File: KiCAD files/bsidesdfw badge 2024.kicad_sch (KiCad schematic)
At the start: 43 parts, among them Q1 BC548, U1 NE555P, U2 74HC595

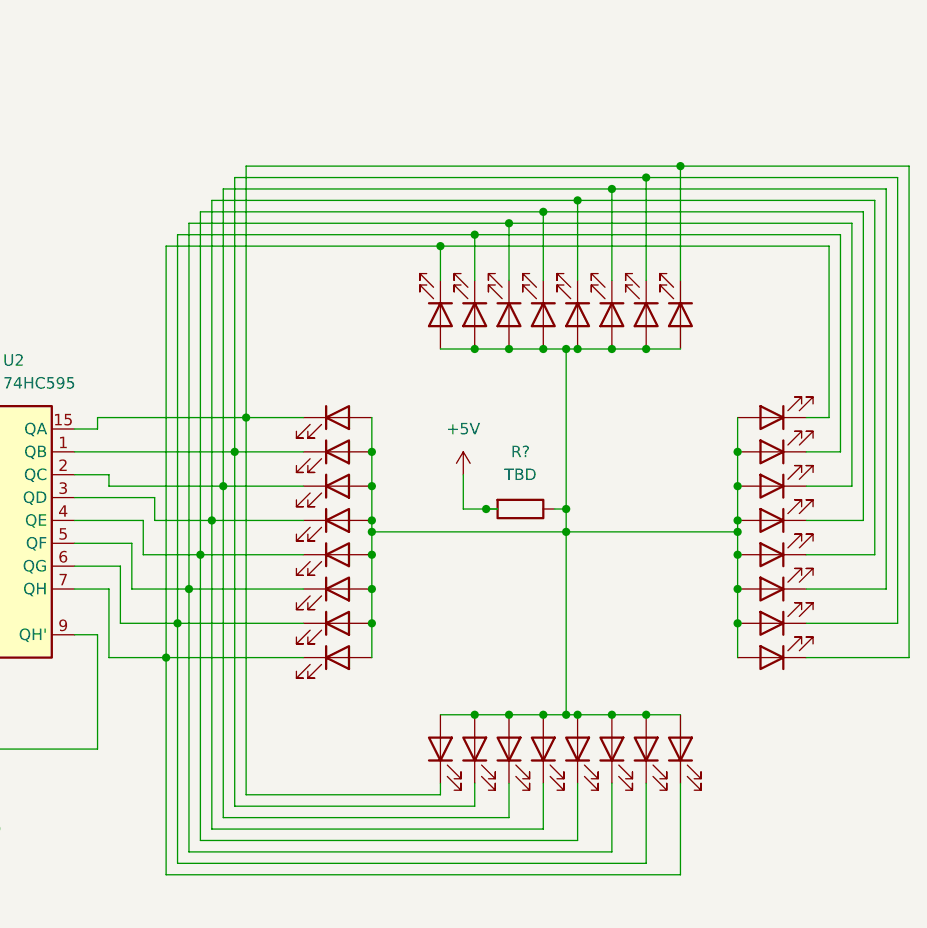
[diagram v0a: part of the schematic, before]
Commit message: updated number of LEDs
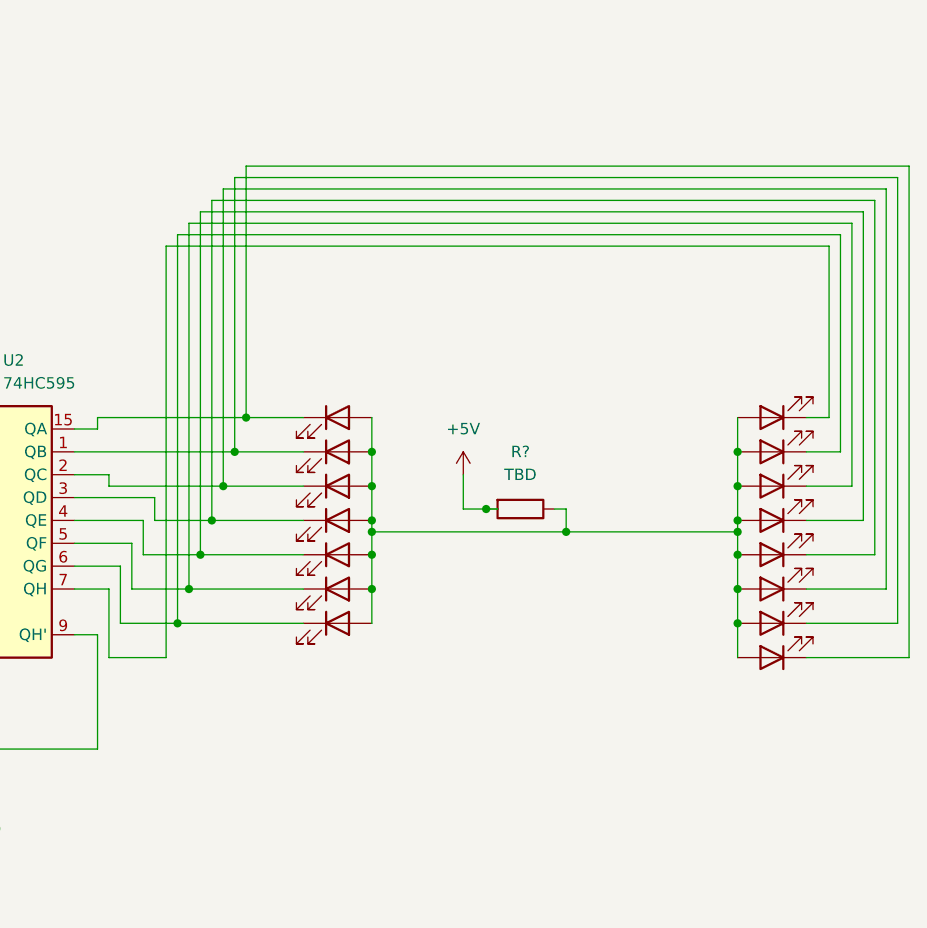
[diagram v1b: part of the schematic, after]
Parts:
- removed D10, D11, D12, D13, D14, D15, D16, D17, D18, D19, D20, D21, D22, D23, D24, D8, D9: ~, symbol Device:LED

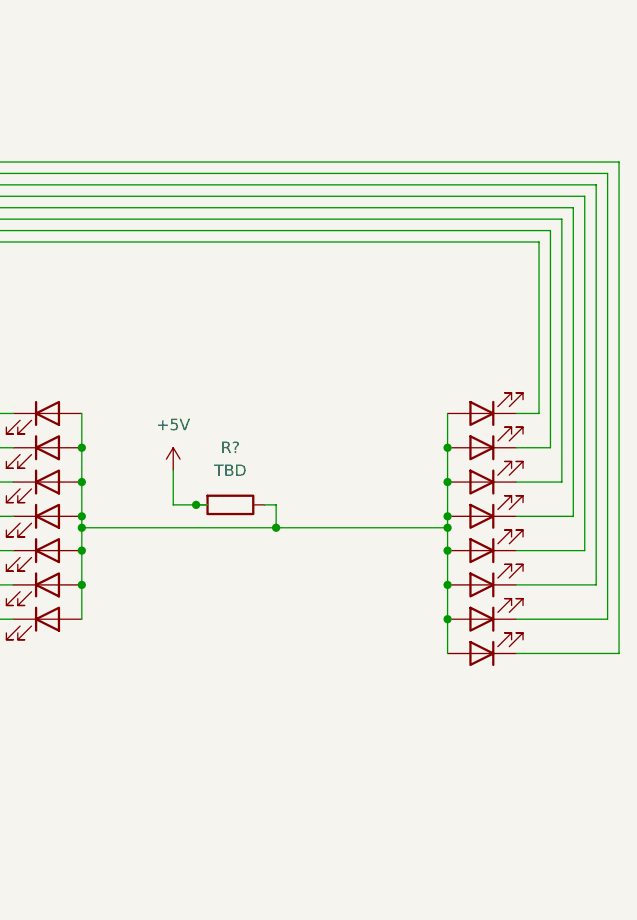
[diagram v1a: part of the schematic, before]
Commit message: LEDs picked, resistor values updated
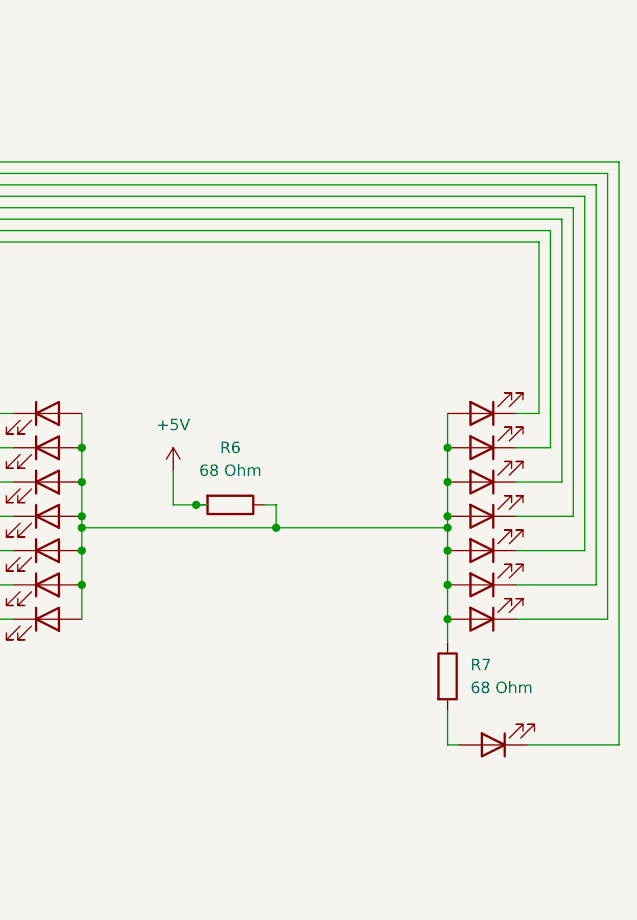
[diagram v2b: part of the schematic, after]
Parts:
- added R7: 68 Ohm, symbol Device:R
- R6: renamed from R?; value TBD -> 68 Ohm
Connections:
- net at D1.2 (A), D2.2 (A), D25.2 (A)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: now also R7.1; no longer D32.2 (A)
- new net: D32.2 (A), R7.2
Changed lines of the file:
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@@
+	)
+	(junction
+		(at 236.22 116.84)
+		(diameter 0)
+		(color 0 0 0 0)
 	)
 	(junction
@@
 	)
 	(junction
-		(at 236.22 116.84)
-		(diameter 0)
-		(color 0 0 0 0)
-	)
-	(junction
 		(at 195.58 109.22)
 		(diameter 0)
@@
 	(wire
 		(pts
+			(xy 236.22 127) (xy 236.22 130.81)
+		)
+		(stroke
+			(width 0)
+			(type default)
+		)
+	)
+	(wire
+		(pts
 			(xy 114.3 130.81) (xy 165.1 130.81)
 		)
@@
 	(wire
 		(pts
+			(xy 236.22 130.81) (xy 237.49 130.81)
+		)
+		(stroke
+			(width 0)
+			(type default)
+		)
+	)
+	(wire
+		(pts
 			(xy 176.53 71.12) (xy 176.53 109.22)
 		)
@@
 	(wire
 		(pts
-			(xy 236.22 116.84) (xy 236.22 120.65)
-		)
-		(stroke
-			(width 0)
-			(type default)
-		)
-	)
-	(wire
-		(pts
 			(xy 173.99 73.66) (xy 247.65 73.66)
 		)
@@
 	(wire
 		(pts
+			(xy 236.22 116.84) (xy 236.22 119.38)
+		)
+		(stroke
+			(width 0)
+			(type default)
+		)
+	)
+	(wire
+		(pts
 			(xy 181.61 93.98) (xy 187.96 93.98)
 		)
@@
 	(wire
 		(pts
-			(xy 255.27 120.65) (xy 255.27 66.04)
-		)
-		(stroke
-			(width 0)
-			(type default)
-		)
-	)
-	(wire
-		(pts
-			(xy 243.84 120.65) (xy 255.27 120.65)
+			(xy 255.27 130.81) (xy 255.27 66.04)
+		)
+		(stroke
+			(width 0)
+			(type default)
+		)
+	)
+	(wire
+		(pts
+			(xy 245.11 130.81) (xy 255.27 130.81)
 		)
 		(stroke
@@
 		(dnp no)
 		(fields_autoplaced yes)
-		(property "Reference" "R?"
+		(property "Reference" "R6"
 			(at 212.09 97.79 90)
 			(effects
@@
 			)
 		)
-		(property "Value" "TBD"
+		(property "Value" "68 Ohm"
 			(at 212.09 100.33 90)
 			(effects
@@
 			(project ""
 				(path "/b322d770-db2f-42fe-b67c-63c256de8558"
-					(reference "R?")
+					(reference "R6")
 					(unit 1)
 				)
@@
 	(symbol
 		(lib_id "Device:R")
+		(at 236.22 123.19 0)
+		(unit 1)
+		(exclude_from_sim no)
+		(in_bom yes)
+		(on_board yes)
+		(dnp no)
+		(fields_autoplaced yes)
+		(property "Reference" "R7"
+			(at 238.76 121.9199 0)
+			(effects
+				(font
+					(size 1.27 1.27)
+				)
+				(justify left)
+			)
+		)
+		(property "Value" "68 Ohm"
+			(at 238.76 124.4599 0)
+			(effects
+				(font
+					(size 1.27 1.27)
+				)
+				(justify left)
+			)
+		)
+		(property "Footprint" ""
+			(at 234.442 123.19 90)
+			(effects
+				(font
+					(size 1.27 1.27)
+				)
+				(hide yes)
+			)
+		)
+		(property "Datasheet" "~"
+			(at 236.22 123.19 0)
+			(effects
+				(font
+					(size 1.27 1.27)
+				)
+				(hide yes)
+			)
+		)
+		(property "Description" "Resistor"
+			(at 236.22 123.19 0)
+			(effects
+				(font
+					(size 1.27 1.27)
+				)
+				(hide yes)
+			)
+		)
+		(pin "1"
+		)
+		(pin "2"
+		)
+		(instances
+			(project "bsidesdfw badge 2024"
+				(path "/b322d770-db2f-42fe-b67c-63c256de8558"
+					(reference "R7")
+					(unit 1)
+				)
+			)
+		)
+	)
+	(symbol
+		(lib_id "Device:R")
 		(at 63.5 116.84 0)
 		(unit 1)
@@
 	(symbol
 		(lib_id "Device:LED")
-		(at 240.03 120.65 180)
+		(at 241.3 130.81 180)
 		(unit 1)
 		(exclude_from_sim no)
@@
 		(fields_autoplaced yes)
 		(property "Reference" "D32"
-			(at 241.6176 123.19 90)
+			(at 242.8876 133.35 90)
 			(effects
 				(font
@@
 		)
 		(property "Value" "~"
-			(at 241.6175 123.19 0)
+			(at 242.8875 133.35 0)
 			(effects
 				(font
@@
 		)
 		(property "Footprint" ""
-			(at 240.03 120.65 0)
+			(at 241.3 130.81 0)
 			(effects
 				(font
@@
 		)
 		(property "Datasheet" "~"
-			(at 240.03 120.65 0)
+			(at 241.3 130.81 0)
 			(effects
 				(font
@@
 		)
 		(property "Description" "Light emitting diode"
-			(at 240.03 120.65 0)
-			(effects
-				(font
+			(at 241.3 130.81 0)
+			(effects
+				(font

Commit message: part models. trim pot needs model created
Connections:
- net +5V renamed +6V
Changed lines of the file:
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@@
 			)
 		)
-		(property "Value" "+5V"
-			(at 116.84 102.87 0)
+		(property "Value" "+6V"
+			(at 120.65 100.33 90)
 			(effects
 				(font
@@
 			)
 		)
-		(property "Value" "+5V"
-			(at 205.74 95.25 0)
-			(effects
-				(font
-					(size 1.27 1.27)
-				)
+		(property "Value" "+6V"
+			(at 208.28 99.0599 0)
+			(effects
+				(font
+					(size 1.27 1.27)
+				)
+				(justify left)
 			)
 		)
@@
 			)
 		)
-		(property "Value" "+5V"
-			(at 152.4 80.01 0)
-			(effects
-				(font
-					(size 1.27 1.27)
-				)
+		(property "Value" "+6V"
+			(at 154.94 83.8199 0)
+			(effects
+				(font
+					(size 1.27 1.27)
+				)
+				(justify left)
 			)
 		)
@@
 			)
 		)
-		(property "Value" "+5V"
-			(at 72.39 99.06 0)
-			(effects
-				(font
-					(size 1.27 1.27)
-				)
-			)
-		)
+		(property "Value" "+6V"
+			(at 74.93 102.8699 0)
+			(effects
+				(font
+					(size 1.27 1.27)
+				)
+				(justify left)
+			)
+		)

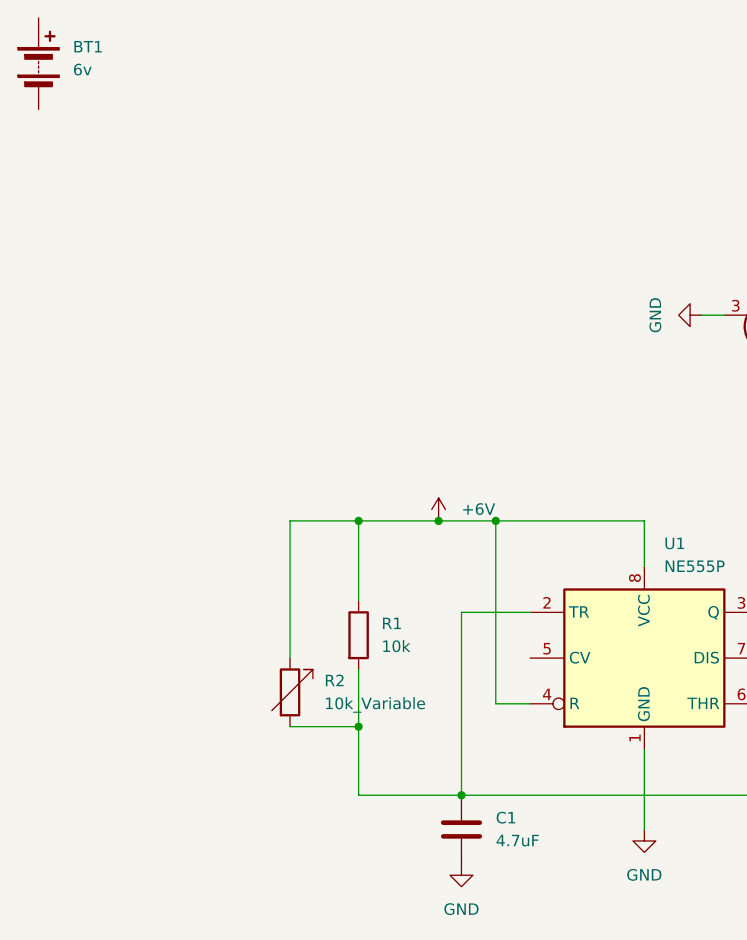
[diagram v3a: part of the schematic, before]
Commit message: corrected the pin numbering for the trim resistor footprint; updated schematic to reflect trim properly
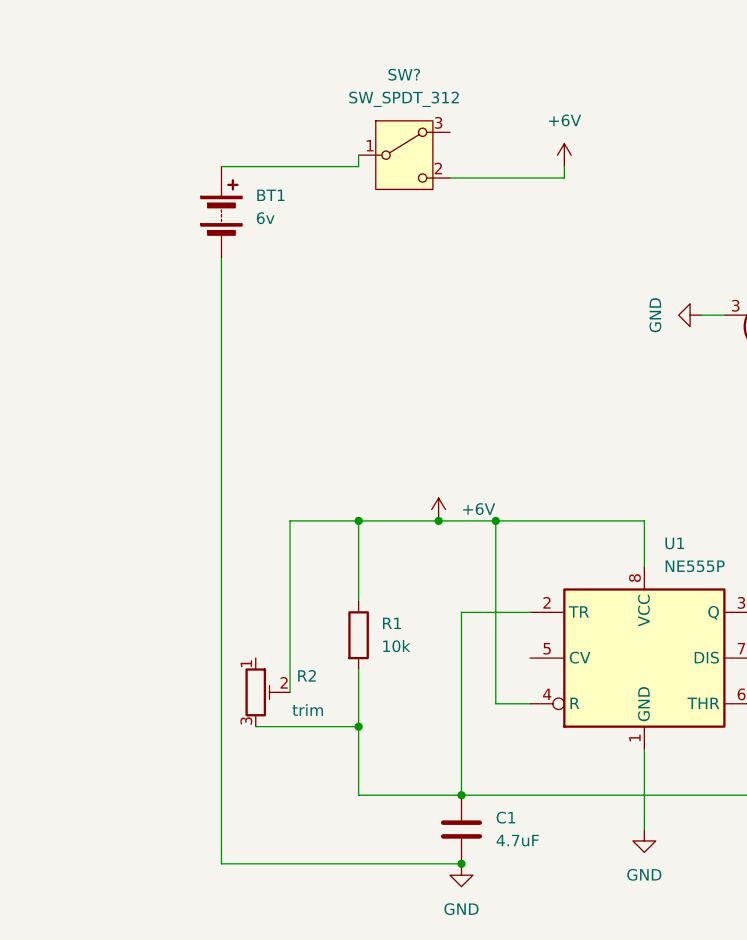
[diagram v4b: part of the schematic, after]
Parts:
- removed R2: 10k_Variable, symbol Device:R_Variable
- added R2: trim, symbol Device:R_Potentiometer_Trim
- added SW?: SW_SPDT_312, symbol Switch:SW_SPDT_312
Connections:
- net +6V: now also R2.2, SW?.2 (C)
- net GND: now also BT1.2 (-)
- net at BT1.1 (+): now also SW?.1 (B)
- net at C1.1, R1.2, U1.2 (TR)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: now also R2.3
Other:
- moved on the sheet: BT1
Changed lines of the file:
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@@
 	)
 	(junction
+		(at 74.93 142.24)
+		(diameter 0)
+		(color 0 0 0 0)
+	)
+	(junction
 		(at 236.22 116.84)
 		(diameter 0)
@@
 	(wire
 		(pts
+			(xy 63.5 64.77) (xy 63.5 63.5)
+		)
+		(stroke
+			(width 0)
+			(type default)
+		)
+	)
+	(wire
+		(pts
 			(xy 236.22 130.81) (xy 237.49 130.81)
 		)
@@
 	(wire
 		(pts
+			(xy 48.26 142.24) (xy 74.93 142.24)
+		)
+		(stroke
+			(width 0)
+			(type default)
+		)
+	)
+	(wire
+		(pts
 			(xy 176.53 71.12) (xy 176.53 109.22)
 		)
@@
 	(wire
 		(pts
+			(xy 48.26 74.93) (xy 48.26 142.24)
+		)
+		(stroke
+			(width 0)
+			(type default)
+		)
+	)
+	(wire
+		(pts
 			(xy 152.4 85.09) (xy 152.4 90.17)
 		)
@@
 	(wire
 		(pts
+			(xy 52.07 127) (xy 63.5 127)
+		)
+		(stroke
+			(width 0)
+			(type default)
+		)
+	)
+	(wire
+		(pts
 			(xy 72.39 104.14) (xy 78.74 104.14)
 		)
@@
 	(wire
 		(pts
-			(xy 63.5 127) (xy 55.88 127)
-		)
-		(stroke
-			(width 0)
-			(type default)
-		)
-	)
-	(wire
-		(pts
 			(xy 107.95 114.3) (xy 129.54 114.3)
 		)
@@
 	(wire
 		(pts
+			(xy 73.66 66.04) (xy 86.36 66.04)
+		)
+		(stroke
+			(width 0)
+			(type default)
+		)
+	)
+	(wire
+		(pts
 			(xy 177.8 69.85) (xy 177.8 105.41)
 		)
@@
 	(wire
 		(pts
+			(xy 48.26 64.77) (xy 63.5 64.77)
+		)
+		(stroke
+			(width 0)
+			(type default)
+		)
+	)
+	(wire
+		(pts
 			(xy 195.58 105.41) (xy 195.58 106.68)
 		)
@@
 	(wire
 		(pts
+			(xy 86.36 66.04) (xy 86.36 64.77)
+		)
+		(stroke
+			(width 0)
+			(type default)
+		)
+	)
+	(wire
+		(pts
 			(xy 123.19 95.25) (xy 123.19 102.87)
 		)
@@
 	(wire
 		(pts
-			(xy 55.88 119.38) (xy 55.88 104.14)
+			(xy 55.88 104.14) (xy 55.88 123.19)
 		)
 		(stroke
@@
 	(symbol
 		(lib_id "Device:Battery")
-		(at 27.94 53.34 0)
+		(at 48.26 69.85 0)
 		(unit 1)
 		(exclude_from_sim no)
@@
 		(fields_autoplaced yes)
 		(property "Reference" "BT1"
-			(at 31.75 51.4984 0)
+			(at 52.07 68.0084 0)
 			(effects
 				(font
@@
 		)
 		(property "Value" "6v"
-			(at 31.75 54.0384 0)
+			(at 52.07 70.5484 0)
 			(effects
 				(font
@@
 		)
 		(property "Footprint" ""
-			(at 27.94 51.816 90)
+			(at 48.26 68.326 90)
 			(effects
 				(font
@@
 		)
 		(property "Datasheet" "~"
-			(at 27.94 51.816 90)
+			(at 48.26 68.326 90)
 			(effects
 				(font
@@
 		)
 		(property "Description" "Multiple-cell battery"
-			(at 27.94 53.34 0)
+			(at 48.26 69.85 0)
 			(effects
 				(font
@@
 	)
 	(symbol
+		(lib_id "power:+5V")
+		(at 86.36 64.77 0)
+		(unit 1)
+		(exclude_from_sim no)
+		(in_bom yes)
+		(on_board yes)
+		(dnp no)
+		(fields_autoplaced yes)
+		(property "Reference" "#PWR09"
+			(at 86.36 68.58 0)
+			(effects
+				(font
+					(size 1.27 1.27)
+				)
+				(hide yes)
+			)
+		)
+		(property "Value" "+6V"
+			(at 86.36 59.69 0)
+			(effects
+				(font
+					(size 1.27 1.27)
+				)
+			)
+		)
+		(property "Footprint" ""
+			(at 86.36 64.77 0)
+			(effects
+				(font
+					(size 1.27 1.27)
+				)
+				(hide yes)
+			)
+		)
+		(property "Datasheet" ""
+			(at 86.36 64.77 0)
+			(effects
+				(font
+					(size 1.27 1.27)
+				)
+				(hide yes)
+			)
+		)
+		(property "Description" "Power symbol creates a global label with name \"+5V\""
+			(at 86.36 64.77 0)
+			(effects
+				(font
+					(size 1.27 1.27)
+				)
+				(hide yes)
+			)
+		)
+		(pin "1"
+		)
+		(instances
+			(project ""
+				(path "/b322d770-db2f-42fe-b67c-63c256de8558"
+					(reference "#PWR09")
+					(unit 1)
+				)
+			)
+		)
+	)
+	(symbol
 		(lib_id "Device:R")
 		(at 236.22 123.19 0)
@@
 	)
 	(symbol
+		(lib_id "Device:R_Potentiometer_Trim")
+		(at 52.07 123.19 0)
+		(unit 1)
+		(exclude_from_sim no)
+		(in_bom yes)
+		(on_board yes)
+		(dnp no)
+		(property "Reference" "R2"
+			(at 58.928 121.412 0)
+			(effects
+				(font
+					(size 1.27 1.27)
+				)
+				(justify right)
+			)
+		)
+		(property "Value" "trim"
+			(at 59.69 125.222 0)
+			(effects
+				(font
+					(size 1.27 1.27)
+				)
+				(justify right)
+			)
+		)
+		(property "Footprint" ""
+			(at 52.07 123.19 0)
+			(effects
+				(font
+					(size 1.27 1.27)
+				)
+				(hide yes)
+			)
+		)
+		(property "Datasheet" "~"
+			(at 52.07 123.19 0)
+			(effects
+				(font
+					(size 1.27 1.27)
+				)
+				(hide yes)
+			)
+		)
+		(property "Description" "Trim-potentiometer"
+			(at 52.07 123.19 0)
+			(effects
+				(font
+					(size 1.27 1.27)
+				)
+				(hide yes)
+			)
+		)
+		(pin "1"
+		)
+		(pin "3"
+		)
+		(pin "2"
+		)
+		(instances
+			(project ""
+				(path "/b322d770-db2f-42fe-b67c-63c256de8558"
+					(reference "R2")
+					(unit 1)
+				)
+			)
+		)
+	)
+	(symbol
 		(lib_id "74xx:74HC595")
 		(at 152.4 105.41 0)
@@
 	)
 	(symbol
+		(lib_id "Switch:SW_SPDT_312")
+		(at 68.58 63.5 0)
+		(unit 1)
+		(exclude_from_sim no)
+		(in_bom yes)
+		(on_board yes)
+		(dnp no)
+		(fields_autoplaced yes)
+		(property "Reference" "SW?"
+			(at 68.58 54.61 0)
+			(effects
+				(font
+					(size 1.27 1.27)
+				)
+			)
+		)
+		(property "Value" "SW_SPDT_312"
+			(at 68.58 57.15 0)
+			(effects
+				(font
+					(size 1.27 1.27)
+				)
+			)
+		)
+		(property "Footprint" ""
+			(at 68.58 73.66 0)
+			(effects
+				(font
+					(size 1.27 1.27)
+				)
+				(hide yes)
+			)
+		)
+		(property "Datasheet" "~"
+			(at 68.58 71.12 0)
+			(effects
+				(font
+					(size 1.27 1.27)
+				)
+				(hide yes)
+			)
+		)
+		(property "Description" "Switch, single pole double throw"
+			(at 68.58 63.5 0)
+			(effects
+				(font
+					(size 1.27 1.27)
+				)
+				(hide yes)
+			)
+		)
+		(pin "1"
+		)
+		(pin "3"
+		)
+		(pin "2"
+		)
+		(instances
+			(project ""
+				(path "/b322d770-db2f-42fe-b67c-63c256de8558"
+					(reference "SW?")
+					(unit 1)
+				)
+			)
+		)
+	)
+	(symbol
 		(lib_id "power:GND")
 		(at 152.4 134.62 0)
@@
 					(unit 1)
 				)
-			)
-		)
-	)
-	(symbol
-		(lib_id "Device:R_Variable")
-		(at 55.88 123.19 0)
-		(unit 1)
-		(exclude_from_sim no)
-		(in_bom yes)
-		(on_board yes)
-		(dnp no)
-		(fields_autoplaced yes)
-		(property "Reference" "R2"
-			(at 59.69 121.9199 0)
-			(effects
-				(font
-					(size 1.27 1.27)
-				)
-				(justify left)
-			)
-		)
-		(property "Value" "10k_Variable"
-			(at 59.69 124.4599 0)
-			(effects
-				(font
-					(size 1.27 1.27)
-				)
-				(justify left)
-			)
-		)
-		(property "Footprint" ""
-			(at 54.102 123.19 90)
-			(effects
-				(font
-					(size 1.27 1.27)
-				)
-				(hide yes)
-			)
-		)
-		(property "Datasheet" "~"
-			(at 55.88 123.19 0)
-			(effects
-				(font
-					(size 1.27 1.27)
-				)
-				(hide yes)
-			)
-		)
-		(property "Description" "Variable resistor"
-			(at 55.88 123.19 0)
-			(effects
-				(font
-					(size 1.27 1.27)
-				)
-				(hide yes)
-			)
-		)
-		(pin "2"
-		)
-		(pin "1"
-		)
-		(instances
-			(project ""
-				(path "/b322d770-db2f-42fe-b67c-63c256de8558"
-					(reference "R2")
-					(unit 1)
-				)
